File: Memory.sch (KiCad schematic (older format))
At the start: 31 parts, among them Q2 2N2222, Q3 2N2222, Q4 2N2222, U13 74HC157, U14 74HC157, U15 74HC08, U16 74HC273, U17 AS6C6264, U18 AT28C64B, U19 AT28C64B, U36 74LS08, U44 74HC193, U45 74HC193

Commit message: For desktop work
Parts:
- added R43, R44, R45, R46, R47, R48, R49, R50, R51, R52, R53, R54, R55, R56, R57, R58, R59, R60, R61, R62, R63, R64, R65, R66: 10k, symbol Device:R
- added U57, U58, U59: ULN2804A, symbol Transistor_Array:ULN2804A
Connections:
- wire segments 288 -> 439
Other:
- moved on the sheet: C18, C19, C28, C29, C30, Q2, R22, R23, R24, U15A, U15B, U15E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

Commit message: Migrated old device part numbers to SN74 LS or HCT series
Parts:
- removed R43, R44, R45, R46, R47, R48, R49, R50, R51, R52, R53, R54, R55, R56, R57, R58, R59, R60, R61, R62, R63, R64, R65, R66: 10k, symbol Device:R
- removed U57, U58, U59: ULN2804A, symbol Transistor_Array:ULN2804A
- U13, U14: value 74HC157 -> 74HCT157N
- U15: value 74HC08 -> 74HCT08N
- U16: value 74HC273 -> 74HCT273N
- U36: value 74LS08 -> 74HCT08N
- U44, U45: value 74HC193 -> 74LS193N
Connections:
- wire segments 439 -> 288

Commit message: Remote work
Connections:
- net INTERRUPT renamed INT
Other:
- note added: "EEPROMs for user\nand interrupt code"
- note added: "Interrupt Stack Pointers"
- note added: "MAR"
- note added: "Mux to choose int \nstack pointer or MAR"
- note added: "SRAM for active use"
- note removed: "SRAM"
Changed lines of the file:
@@
 Text Notes 11175 7425 0    50   ~ 0
 EEPROM
-Text Notes 11950 2850 0    50   ~ 0
-SRAM
 $Comp
 L 74xx:74AHCT273 U16
@@
 Connection ~ 11350 8350
 Text HLabel 9800 7300 0    50   Input ~ 0
-INTERRUPT
+INT
 Wire Wire Line
 	9950 7600 10100 7600
@@
 	10000 5650 10100 5650
 Text HLabel 9800 5350 0    50   Input ~ 0
-INTERRUPT
+INT
 Entry Wire Line
 	9850 6550 9950 6450
@@
 Text HLabel 10950 7850 2    50   Output ~ 0
 I15
+Text Notes 1850 4950 0    118  ~ 0
+Interrupt Stack Pointers
+Text Notes 5275 2550 0    118  ~ 0
+MAR
+Text Notes 6775 2250 0    118  ~ 0
+Mux to choose int \nstack pointer or MAR
 Wire Bus Line
 	8400 3000 8400 8600
@@
 Wire Bus Line
 	9850 3950 9850 8600
+Text Notes 9850 2125 0    118  ~ 0
+SRAM for active use
+Text Notes 11625 6950 0    118  ~ 0
+EEPROMs for user\nand interrupt code
 $EndSCHEMATC

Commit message: Replaced all broken schematics with the up-to-date versions.  Some symbols missing.  This version will be the one created IRL except for the carry flag.
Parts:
- removed C19, C29, C42, C43: 0.1u, symbol Device:C_Small
- removed C40, C41: 1n, symbol Device:C_Small
- removed Q3, Q4: 2N2222, symbol Device:Q_NPN_CBE
- removed R20, R21, R25, R26: 10k, symbol Device:R
- removed R27, R28: 200, symbol Device:R
- removed U13, U14: 74HCT157N, symbol 74xx:74LS157
- removed U15, U36: 74HCT08N, symbol 74xx:74LS08
- removed U19: AT28C64B, symbol Memory:AT28C64B
- removed U44, U45: 74LS193N, symbol 74xx:74LS193
- added C402, C403, C404, C405, C406, C407, C409, C412, C413, C414: 0.1u, symbol Breadboard_CPU-rescue:C_Small-Device
- added Q402: 2N2222, symbol Breadboard_CPU-rescue:Q_NPN_CBE-Device
- added R402: 4.7k, symbol Breadboard_CPU-rescue:R-Device
- added R405, R422, R423, R424, R425, R426, R427, R428, R429: 10k, symbol Breadboard_CPU-rescue:R-Device
- added R406, R407, R408, R409, R410, R411, R412, R413, R414, R415, R416, R417, R418, R419, R420, R421: 1k, symbol Breadboard_CPU-rescue:R-Device
- added U401, U408: 74HCT74N, symbol Breadboard_CPU-rescue:74LS74-74xx
- added U402, U403, U406: 74HCT08N, symbol Breadboard_CPU-rescue:74LS08-74xx
- added U404: 74LS04, symbol Breadboard_CPU-rescue:74LS04-74xx
- added U407: 74HCT138N, symbol Breadboard_CPU-rescue:74LS138-74xx
- added U410: 74HCT273N, symbol Breadboard_CPU-rescue:74AHCT273-74xx
- added U411, U414: 74HCT32N, symbol Breadboard_CPU-rescue:74LS32-74xx
- added U415, U416: 74HCT574N, symbol Breadboard_CPU-rescue:74HCT574-74xx
- added U417: 74HCT541N, symbol Breadboard_CPU-rescue:74HCT541-74xx
- C408: renamed from C28; symbol Device:C_Small -> Breadboard_CPU-rescue:C_Small-Device
- C410: renamed from C18; value 1n -> 0.1n; symbol Device:C_Small -> Breadboard_CPU-rescue:C_Small-Device
- C411: renamed from C30; symbol Device:C_Small -> Breadboard_CPU-rescue:C_Small-Device
- Q401: renamed from Q2; symbol Device:Q_NPN_CBE -> Breadboard_CPU-rescue:Q_NPN_CBE-Device
- R401: renamed from R22; value 470 -> 4.7k; symbol Device:R -> Breadboard_CPU-rescue:R-Device
- R403: renamed from R23; symbol Device:R -> Breadboard_CPU-rescue:R-Device
- R404: renamed from R24; symbol Device:R -> Breadboard_CPU-rescue:R-Device
- U409: renamed from U16; symbol 74xx:74AHCT273 -> Breadboard_CPU-rescue:74AHCT273-74xx
- renumbered U18 to U412, U17 to U413
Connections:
- net labels added: CLK_MAR_IN, CLK_MEM_IN, MAR[0], MAR[10], MAR[11], MAR[12], MAR[13], MAR[14], MAR[15], MAR[1], MAR[2], MAR[3], MAR[4], MAR[5], MAR[6], MAR[7], MAR[8], MAR[9], PA_SEL, PB_MODE, PB_SEL, ~CLK, ~PA_SEL, ~PB_IN, ~PB_SEL
- net labels removed: A0, A1, A2, A3, A4, A5, A6, A7, D0, D1, D2, D3, D4, D5, D6, D7, ETI_RTI, I0, I1, I10, I11, I12, I13, I14, I15, I2, I3, I4, I5, I6, I7, I8, I9, INT, Q0, Q1, Q2, Q3, Q4, Q5, Q6, Q7, RST, STKPTR_DEC, STKPTR_INC
- wire segments 288 -> 392
- no-connect marks 10 -> 6
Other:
- note added: "Chip active for MAR[15:0] = 16'b1111 1 xxx xxxx xxxx"
- note added: "EEPROM for user\nand OS code"
- note added: "High byte\n"
- note added: "Initial state: 0b0\nAfter MAR_IN rises 1x: 0b1 (ready to read in high byte)\nAfter MAR_IN rises 2x: 0b0 (ready to read in low byte)\nAt 3x, this tff has cycled to the first MAR_IN rising condition\n"
- note added: "Low byte"
- note added: "Port A\n(usually only\nfor output)"
- note added: "Port B\n(usually used for\ndata transfer)"
- note added: "SRAM for active use (16 KB available)"
- note added: "Set Px_MODE to 0\nfor the ports to be on\nOUTPUT mode"
- note added: "When MEM_OUT and MAR[15] go low, we are accessing the code EEPROM\nToggle the"
- note removed: "EEPROM"
- note removed: "EEPROMs for user\nand interrupt code"
- note removed: "Interrupt Stack Pointers"
- note removed: "Mux to choose int \nstack pointer or MAR"
- note removed: "SRAM for active use"
- moved on the sheet: C408, C410, C411, Q401, R401, R403, R404, U409, U412, U413

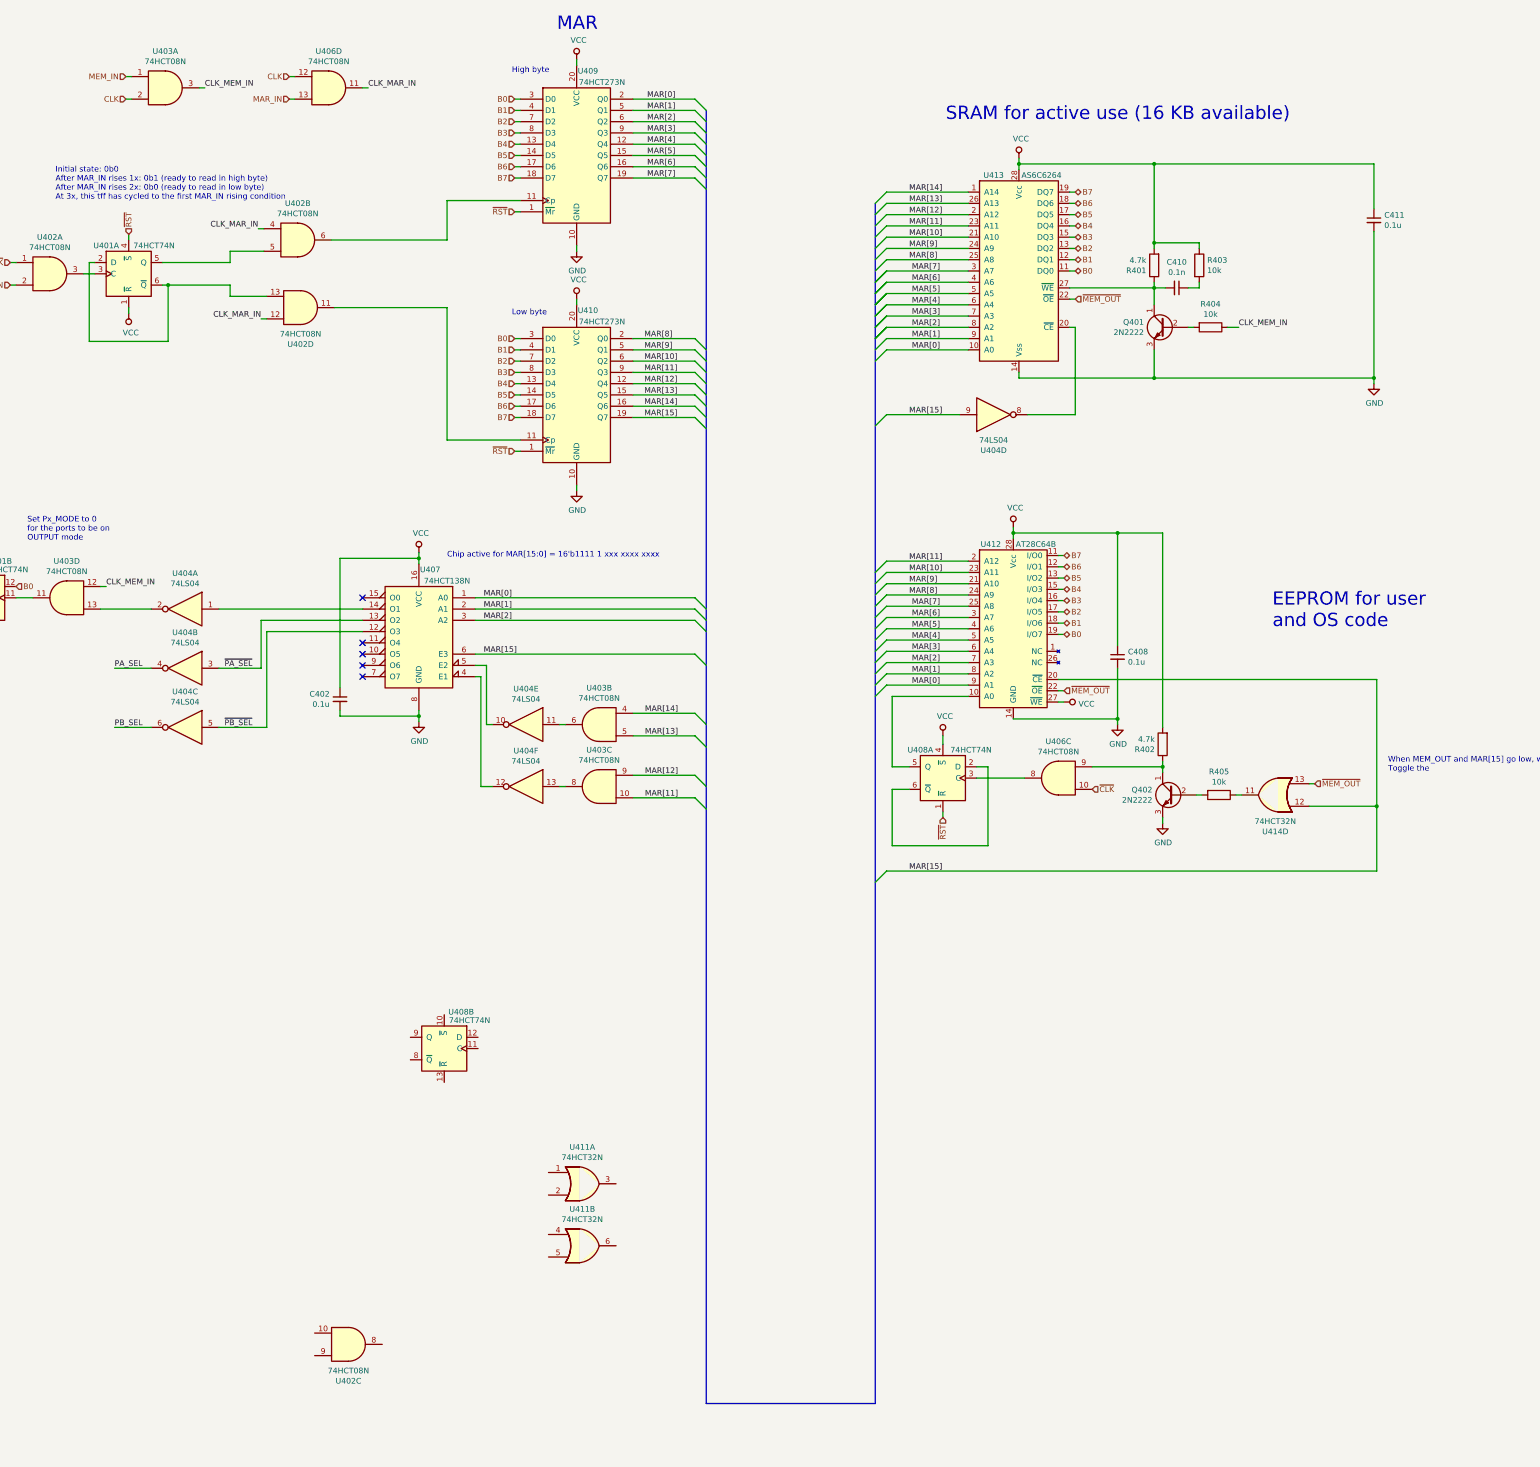
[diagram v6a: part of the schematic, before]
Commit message: Rearranged some generic logic gates in ALU to match physical net connections on the breadboard.
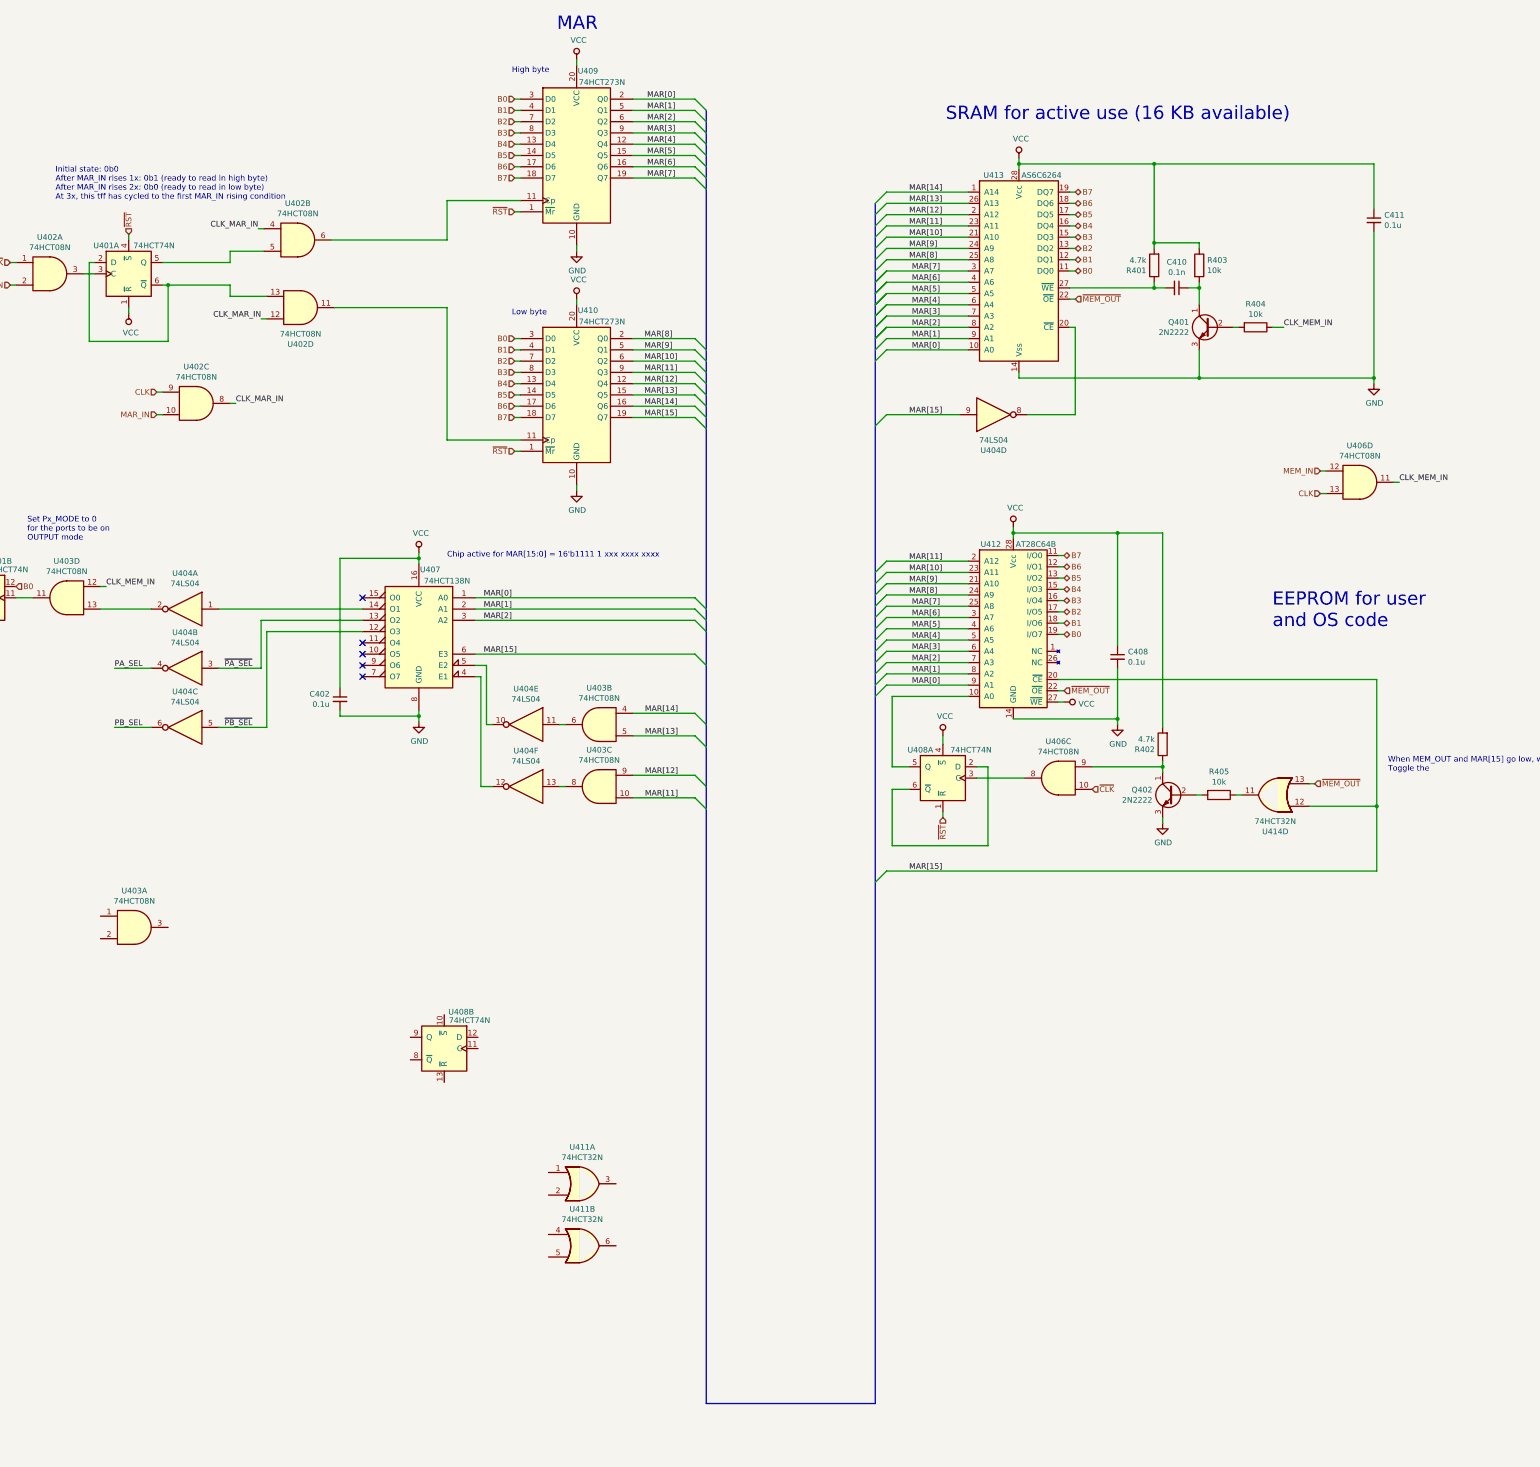
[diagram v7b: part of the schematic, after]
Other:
- moved on the sheet: Q401, R404, U402C, U403A, U406D
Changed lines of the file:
@@
 L Breadboard_CPU-rescue:Q_NPN_CBE-Device Q401
 U 1 1 5F79CEAE
-P 11700 3375
-F 0 "Q401" H 11891 3421 50  0000 L CNN
-F 1 "2N2222" H 11891 3330 50  0000 L CNN
-F 2 "" H 11900 3475 50  0001 C CNN
-F 3 "~" H 11700 3375 50  0001 C CNN
-	1    11700 3375
+P 12100 3375
+F 0 "Q401" H 12291 3421 50  0000 L CNN
+F 1 "2N2222" H 12291 3330 50  0000 L CNN
+F 2 "" H 12300 3475 50  0001 C CNN
+F 3 "~" H 12100 3375 50  0001 C CNN
+	1    12100 3375
 	-1   0    0    -1
 $EndComp
 Wire Wire Line
-	11600 3175 11600 3025
+	12000 3175 12000 3025
 Connection ~ 11600 3025
 Wire Wire Line
-	11600 3575 11600 3825
+	12000 3575 12000 3825
 Wire Wire Line
 	10850 3025 11600 3025
 Wire Wire Line
-	11900 3375 11950 3375
-Text HLabel 2475 1350 0    50   Input ~ 0
+	12300 3375 12350 3375
+Text HLabel 13075 4850 0    50   Input ~ 0
 CLK
 Wire Wire Line
-	2525 1350 2475 1350
-Text HLabel 2475 1150 0    50   Input ~ 0
+	13125 4850 13075 4850
+Text HLabel 13075 4650 0    50   Input ~ 0
 MEM_IN
 Wire Wire Line
-	2475 1150 2525 1150
+	13075 4650 13125 4650
 $Comp
 L Breadboard_CPU-rescue:C_Small-Device C408
@@
 	9225 3175 9125 3275
 Wire Wire Line
-	11600 3825 13550 3825
-Connection ~ 11600 3825
-Wire Wire Line
 	10400 3775 10400 3825
 $Comp
 L Breadboard_CPU-rescue:R-Device R404
 U 1 1 5FACF7B8
-P 12100 3375
-F 0 "R404" V 11893 3375 50  0000 C CNN
-F 1 "10k" V 11984 3375 50  0000 C CNN
-F 2 "" V 12030 3375 50  0001 C CNN
-F 3 "~" H 12100 3375 50  0001 C CNN
-	1    12100 3375
+P 12500 3375
+F 0 "R404" V 12293 3375 50  0000 C CNN
+F 1 "10k" V 12384 3375 50  0000 C CNN
+F 2 "" V 12430 3375 50  0001 C CNN
+F 3 "~" H 12500 3375 50  0001 C CNN
+	1    12500 3375
 	0    1    1    0
 $EndComp
@@
 $EndComp
 Wire Wire Line
-	3925 1350 3975 1350
+	2750 4150 2800 4150
 Wire Wire Line
 	5925 4475 5975 4475
@@
 L Breadboard_CPU-rescue:74LS08-74xx U?
 U 1 1 61B1F14E
-P 2825 1250
+P 2550 8700
 AR Path="/5EFC06D4/61B1F14E" Ref="U?"  Part="1"
 AR Path="/5EFC0623/61B1F14E" Ref="U403"  Part="1"
-F 0 "U403" H 2825 1575 50  0000 C CNN
-F 1 "74HCT08N" H 2825 1484 50  0000 C CNN
-F 2 "" H 2825 1250 50  0001 C CNN
-F 3 "http://www.ti.com/lit/gpn/sn74LS08" H 2825 1250 50  0001 C CNN
-	1    2825 1250
+F 0 "U403" H 2550 9025 50  0000 C CNN
+F 1 "74HCT08N" H 2550 8934 50  0000 C CNN
+F 2 "" H 2550 8700 50  0001 C CNN
+F 3 "http://www.ti.com/lit/gpn/sn74LS08" H 2550 8700 50  0001 C CNN
+	1    2550 8700
 	1    0    0    -1
 $EndComp
@@
 Entry Wire Line
 	7525 1350 7625 1450
-Text HLabel 3925 1350 0    50   Input ~ 0
+Text HLabel 2750 4150 0    50   Input ~ 0
 MAR_IN
 Wire Wire Line
@@
 	9225 4150 9875 4150
 Wire Wire Line
-	10400 3825 11600 3825
-Wire Wire Line
 	10900 3375 10900 4150
 Wire Wire Line
@@
 L Breadboard_CPU-rescue:74LS08-74xx U?
 U 4 1 60A654AA
-P 4275 1250
+P 13425 4750
 AR Path="/5EFC06D4/60A654AA" Ref="U?"  Part="4"
 AR Path="/619E6F28/60A654AA" Ref="U?"  Part="4"
 AR Path="/5EFC0623/60A654AA" Ref="U406"  Part="4"
-F 0 "U406" H 4275 1575 50  0000 C CNN
-F 1 "74HCT08N" H 4275 1484 50  0000 C CNN
-F 2 "" H 4275 1250 50  0001 C CNN
-F 3 "http://www.ti.com/lit/gpn/sn74LS08" H 4275 1250 50  0001 C CNN
-	4    4275 1250
+F 0 "U406" H 13425 5075 50  0000 C CNN
+F 1 "74HCT08N" H 13425 4984 50  0000 C CNN
+F 2 "" H 13425 4750 50  0001 C CNN
+F 3 "http://www.ti.com/lit/gpn/sn74LS08" H 13425 4750 50  0001 C CNN
+	4    13425 4750
 	1    0    0    -1
 $EndComp
@@
 	3300 5875 4575 5875
 Wire Wire Line
-	3125 1250 3175 1250
-Text Label 3175 1250 0    50   ~ 0
+	13725 4750 13775 4750
+Text Label 13775 4750 0    50   ~ 0
 CLK_MEM_IN
-Text Label 12350 3375 0    50   ~ 0
+Text Label 12750 3375 0    50   ~ 0
 CLK_MEM_IN
 Wire Wire Line
-	12250 3375 12350 3375
+	12650 3375 12750 3375
 Wire Wire Line
 	2250 5675 2300 5675
@@
 When MEM_OUT and MAR[15] go low, we are accessing the code EEPROM\nToggle the
 Wire Wire Line
-	3925 1150 3975 1150
-Text HLabel 3925 1150 0    50   Input ~ 0
+	2750 3950 2800 3950
+Text HLabel 2750 3950 0    50   Input ~ 0
 CLK
 $Comp
@@
 Text Label 16125 10075 2    50   ~ 0
 CLK_MEM_IN
-Text Label 4625 1250 0    50   ~ 0
+Text Label 3450 4050 0    50   ~ 0
 CLK_MAR_IN
 Wire Wire Line
@@
 Connection ~ 2850 3000
 Wire Wire Line
-	4575 1250 4625 1250
+	3400 4050 3450 4050
 Text Label 3675 3300 2    50   ~ 0
 CLK_MAR_IN
@@
 L Breadboard_CPU-rescue:74LS08-74xx U?
 U 3 1 61B1F15A
-P 4450 12400
+P 3100 4050
 AR Path="/5EFC06D4/61B1F15A" Ref="U?"  Part="3"
 AR Path="/5EFC0623/61B1F15A" Ref="U402"  Part="3"
-F 0 "U402" H 4450 12725 50  0000 C CNN
-F 1 "74HCT08N" H 4450 12634 50  0000 C CNN
-F 2 "" H 4450 12400 50  0001 C CNN
-F 3 "http://www.ti.com/lit/gpn/sn74LS08" H 4450 12400 50  0001 C CNN
-	3    4450 12400
-	1    0    0    1
+F 0 "U402" H 3100 4375 50  0000 C CNN
+F 1 "74HCT08N" H 3100 4284 50  0000 C CNN
+F 2 "" H 3100 4050 50  0001 C CNN
+F 3 "http://www.ti.com/lit/gpn/sn74LS08" H 3100 4050 50  0001 C CNN
+	3    3100 4050
+	1    0    0    -1
 $EndComp
 $Comp
@@
 Text HLabel 1450 2800 0    50   Input ~ 0
 ~CLK
+Connection ~ 12000 3025
+Connection ~ 12000 3825
+Wire Wire Line
+	12000 3825 13550 3825
+Wire Wire Line
+	10400 3825 12000 3825
 Wire Bus Line
 	9125 2275 9125 12925

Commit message: Libraries re-imported.  Using rescue symbols still.  Adjusted multi-byte registers to use low-byte first.. applied this convention to all multi-byte registers for consistency.
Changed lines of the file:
@@
 Text Notes 1850 2250 0    50   ~ 0
 Initial state: 0b0\nAfter MAR_IN rises 1x: 0b1 (ready to read in high byte)\nAfter MAR_IN rises 2x: 0b0 (ready to read in low byte)\nAt 3x, this tff has cycled to the first MAR_IN rising condition\n
-Text HLabel 2500 2550 1    50   Input ~ 0
+Text HLabel 2500 3250 3    50   Input ~ 0
 ~RST
 Wire Wire Line
-	2500 2550 2500 2600
+	2500 3250 2500 3200
 $Comp
 L Breadboard_CPU-rescue:VCC-power #PWR0402
 U 1 1 5FE5F94F
-P 2500 3250
-F 0 "#PWR0402" H 2500 3100 50  0001 C CNN
-F 1 "VCC" H 2518 3423 50  0000 C CNN
-F 2 "" H 2500 3250 50  0001 C CNN
-F 3 "" H 2500 3250 50  0001 C CNN
-	1    2500 3250
-	1    0    0    1
+P 2500 2550
+F 0 "#PWR0402" H 2500 2400 50  0001 C CNN
+F 1 "VCC" H 2518 2723 50  0000 C CNN
+F 2 "" H 2500 2550 50  0001 C CNN
+F 3 "" H 2500 2550 50  0001 C CNN
+	1    2500 2550
+	-1   0    0    -1
 $EndComp
 Wire Wire Line
-	2500 3200 2500 3250
+	2500 2600 2500 2550
 Text Notes 5900 3275 0    50   ~ 0
 Low byte
